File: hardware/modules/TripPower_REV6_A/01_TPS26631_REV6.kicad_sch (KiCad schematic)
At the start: 13 parts, among them Q201 SQM100N10-10_GE3 100V AEC, Q202 BSS138LT1G DRIVER PULLDOWN, U201 TPS26631PWPR

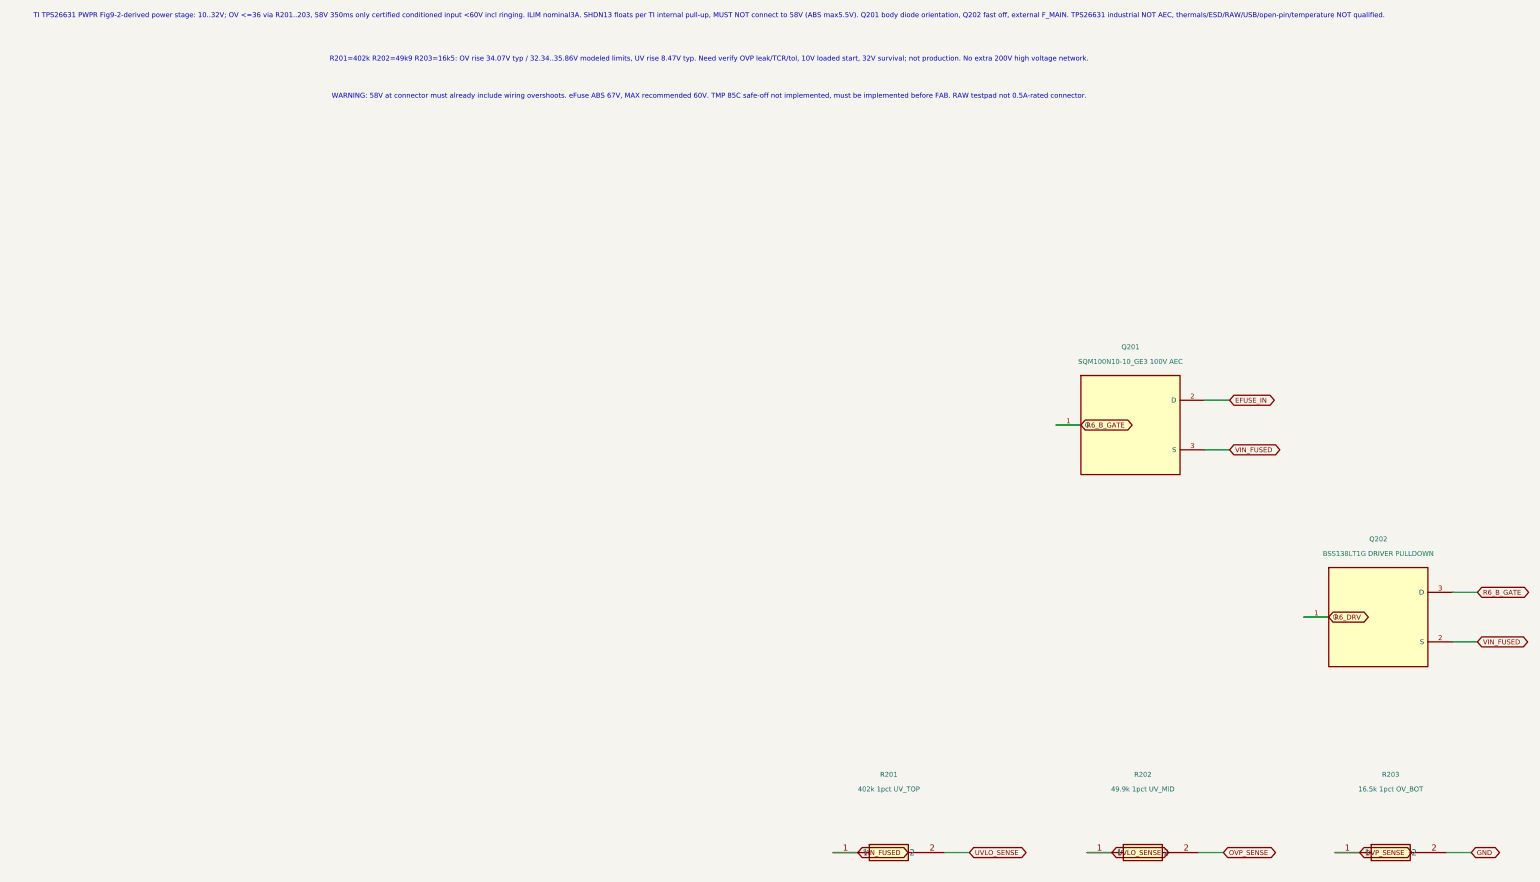
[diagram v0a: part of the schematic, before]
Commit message: Weg A REV6: replace 1% OV divider with available Yageo 0.1% 25ppm 100k/12k4/4k22 to permit verified static 32V OV restart
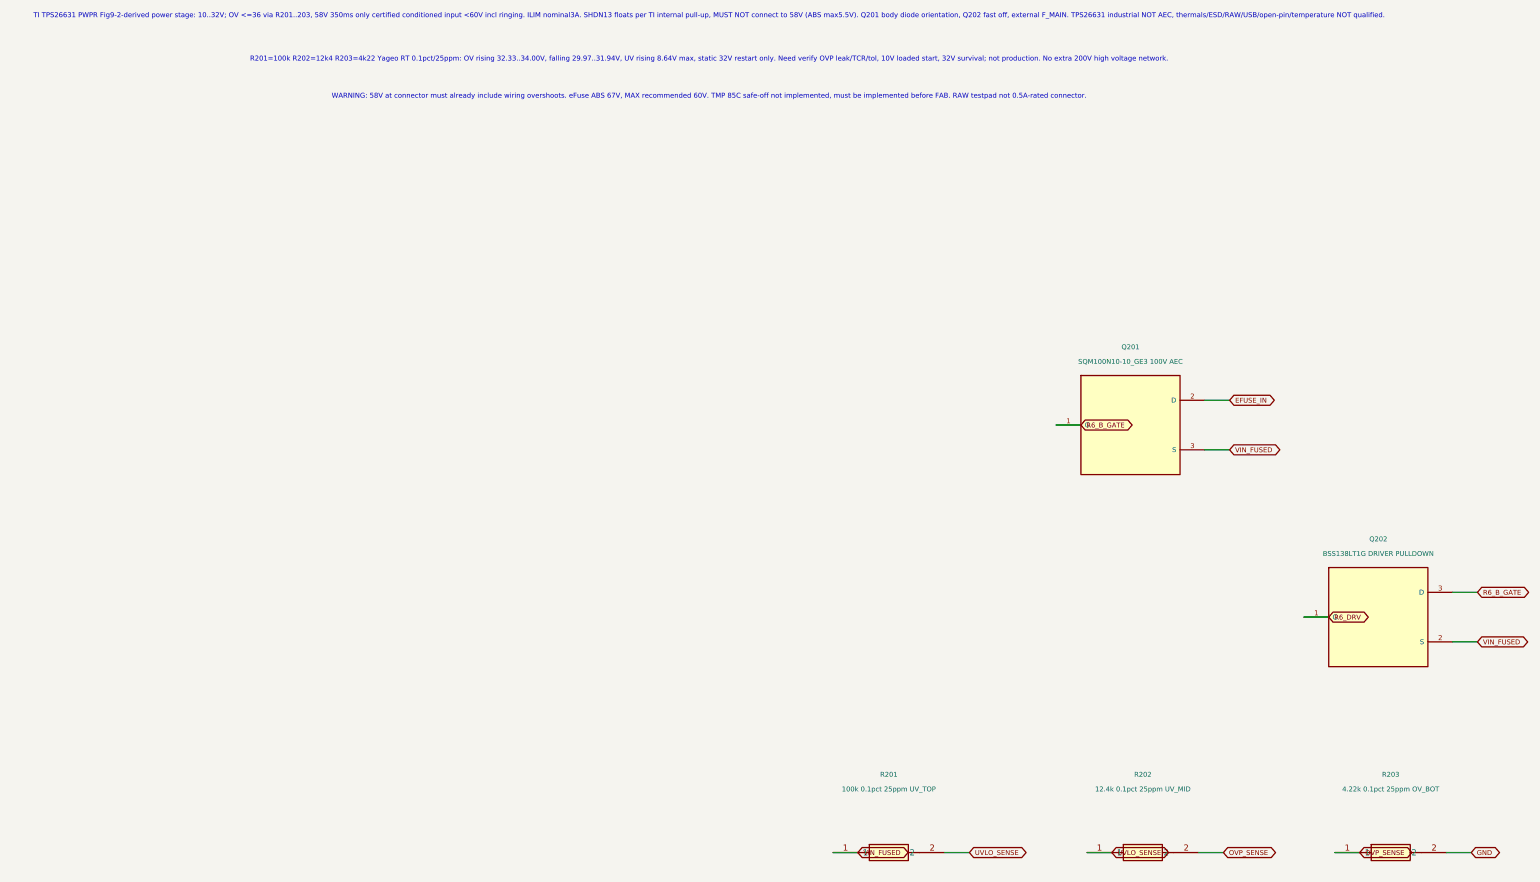
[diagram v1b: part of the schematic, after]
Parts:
- R201: value 402k 1pct UV_TOP -> 100k 0.1pct 25ppm UV_TOP; MPN AC1206FR-07402KL -> RT1206BRD07100KL
- R202: value 49.9k 1pct UV_MID -> 12.4k 0.1pct 25ppm UV_MID; MPN AC1206FR-0749K9L -> RT1206BRD0712K4L
- R203: value 16.5k 1pct OV_BOT -> 4.22k 0.1pct 25ppm OV_BOT; MPN AC1206FR-0716K5L -> RT1206BRD074K22L
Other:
- note added: "R201=100k R202=12k4 R203=4k22 Yageo RT 0.1pct/25ppm: OV rising 32.33..34.00V, falling 29.97..31.94V, UV rising 8.64V max, static 32V restart only. Need verify OVP leak/TCR/tol, 10V loaded start, 32V survival; not production. No extra 200V high voltage network."
- note removed: "R201=402k R202=49k9 R203=16k5: OV rise 34.07V typ / 32.34..35.86V modeled limits, UV rise 8.47V typ. Need verify OVP leak/TCR/tol, 10V loaded start, 32V survival; not production. No extra 200V high voltage network."
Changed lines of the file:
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@@
 (title_block (title "TripPower REV6 A - TPS26631 60V eFuse and 100V reverse FET") (date "2026-10-15") (rev "SCHEMATIC EXPERIMENT / NO FAB"))
 (text "TI TPS26631 PWPR Fig9-2-derived power stage: 10..32V; OV <=36 via R201..203, 58V 350ms only certified conditioned input <60V incl ringing. ILIM nominal3A. SHDN13 floats per TI internal pull-up, MUST NOT connect to 58V (ABS max5.5V). Q201 body diode orientation, Q202 fast off, external F_MAIN. TPS26631 industrial NOT AEC, thermals/ESD/RAW/USB/open-pin/temperature NOT qualified." (at 27.94 34.29 0) (effects (font (size 1.016 1.016))))
-(text "R201=402k R202=49k9 R203=16k5: OV rise 34.07V typ / 32.34..35.86V modeled limits, UV rise 8.47V typ. Need verify OVP leak/TCR/tol, 10V loaded start, 32V survival; not production. No extra 200V high voltage network." (at 27.94 43.18 0) (effects (font (size 1.016 1.016))))
+(text "R201=100k R202=12k4 R203=4k22 Yageo RT 0.1pct/25ppm: OV rising 32.33..34.00V, falling 29.97..31.94V, UV rising 8.64V max, static 32V restart only. Need verify OVP leak/TCR/tol, 10V loaded start, 32V survival; not production. No extra 200V high voltage network." (at 27.94 43.18 0) (effects (font (size 1.016 1.016))))
 (text "WARNING: 58V at connector must already include wiring overshoots. eFuse ABS 67V, MAX recommended 60V. TMP 85C safe-off not implemented, must be implemented before FAB. RAW testpad not 0.5A-rated connector." (at 27.94 50.8 0) (effects (font (size 1.016 1.016))))
 (symbol (lib_id "TripPower_REV6:TPS26631_PWP20") (at 248.92 127 0) (unit 1) (in_bom yes) (on_board yes) (dnp no)
@@
 (symbol (lib_id "Tripmaster_Sym:R") (at 64.77 205.74 0) (unit 1) (in_bom yes) (on_board yes) (dnp no)
 (property "Reference" "R201" (at 64.77 189.74 0) (effects (font (size 1 1))))
-(property "Value" "402k 1pct UV_TOP" (at 64.77 192.74 0) (effects (font (size 1 1))))
+(property "Value" "100k 0.1pct 25ppm UV_TOP" (at 64.77 192.74 0) (effects (font (size 1 1))))
 (property "Footprint" "Resistor_SMD:R_1206_3216Metric" (at 64.77 205.74 0) (effects (font (size 1 1)) (hide yes)))
-(property "MPN" "AC1206FR-07402KL" (at 0 0 0) (effects (font (size 1 1)) (hide yes)))
+(property "MPN" "RT1206BRD07100KL" (at 0 0 0) (effects (font (size 1 1)) (hide yes)))
 (pin "1")
 (pin "2")
@@
 (symbol (lib_id "Tripmaster_Sym:R") (at 116.84 205.74 0) (unit 1) (in_bom yes) (on_board yes) (dnp no)
 (property "Reference" "R202" (at 116.84 189.74 0) (effects (font (size 1 1))))
-(property "Value" "49.9k 1pct UV_MID" (at 116.84 192.74 0) (effects (font (size 1 1))))
+(property "Value" "12.4k 0.1pct 25ppm UV_MID" (at 116.84 192.74 0) (effects (font (size 1 1))))
 (property "Footprint" "Resistor_SMD:R_1206_3216Metric" (at 116.84 205.74 0) (effects (font (size 1 1)) (hide yes)))
-(property "MPN" "AC1206FR-0749K9L" (at 0 0 0) (effects (font (size 1 1)) (hide yes)))
+(property "MPN" "RT1206BRD0712K4L" (at 0 0 0) (effects (font (size 1 1)) (hide yes)))
 (pin "1")
 (pin "2")
@@
 (symbol (lib_id "Tripmaster_Sym:R") (at 167.64 205.74 0) (unit 1) (in_bom yes) (on_board yes) (dnp no)
 (property "Reference" "R203" (at 167.64 189.74 0) (effects (font (size 1 1))))
-(property "Value" "16.5k 1pct OV_BOT" (at 167.64 192.74 0) (effects (font (size 1 1))))
+(property "Value" "4.22k 0.1pct 25ppm OV_BOT" (at 167.64 192.74 0) (effects (font (size 1 1))))
 (property "Footprint" "Resistor_SMD:R_1206_3216Metric" (at 167.64 205.74 0) (effects (font (size 1 1)) (hide yes)))
-(property "MPN" "AC1206FR-0716K5L" (at 0 0 0) (effects (font (size 1 1)) (hide yes)))
+(property "MPN" "RT1206BRD074K22L" (at 0 0 0) (effects (font (size 1 1)) (hide yes)))
 (pin "1")
 (pin "2")

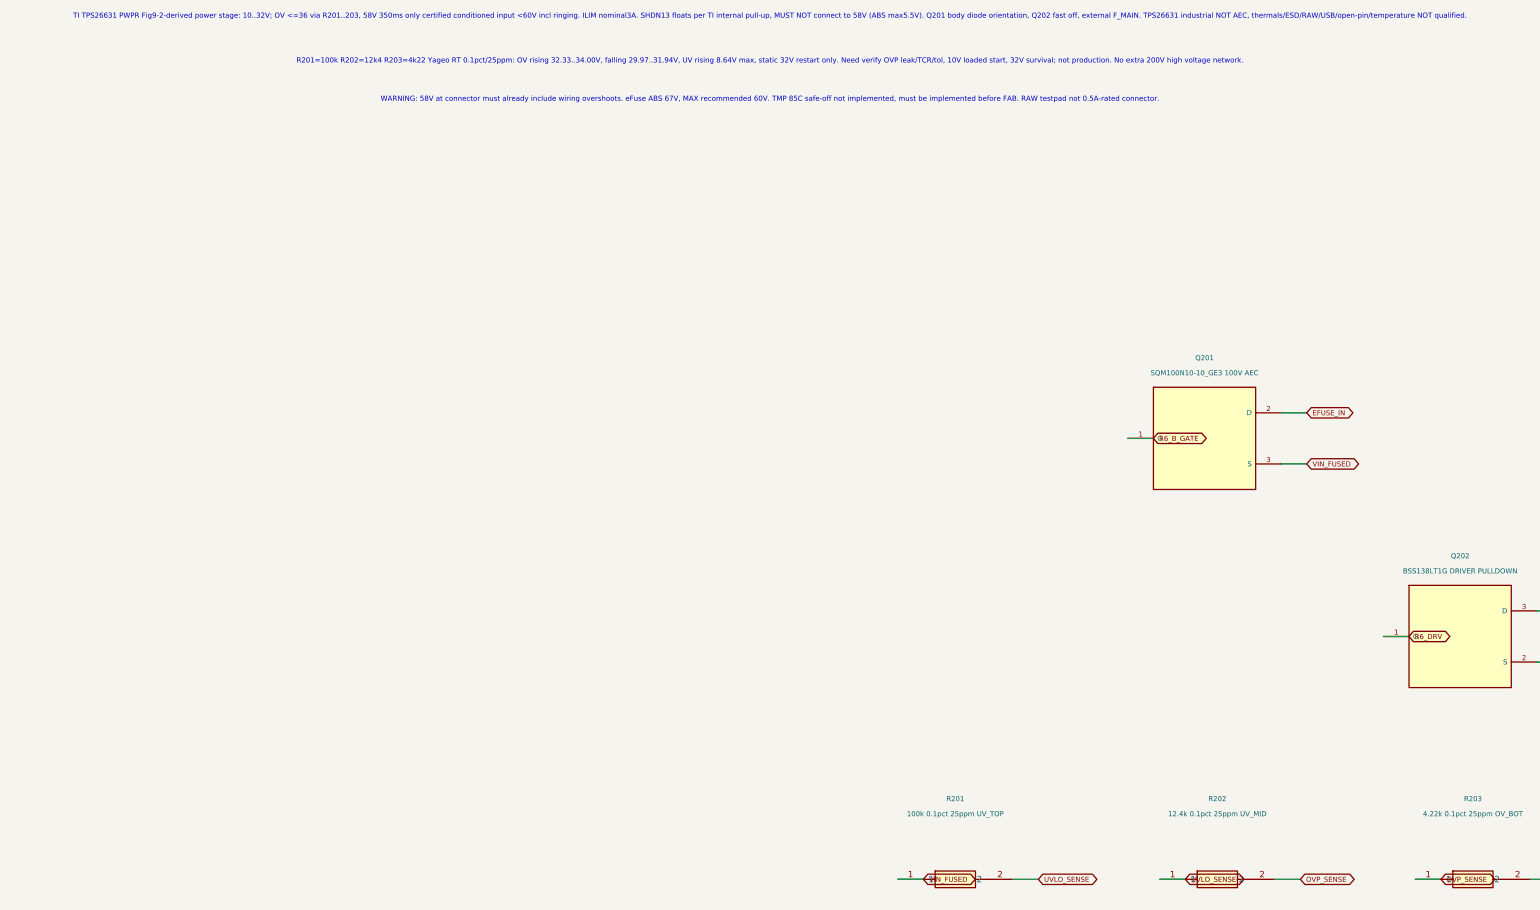
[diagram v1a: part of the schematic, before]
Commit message: TripPower REV6 A: improve 32V OVP return margin using stocked Yageo precision 12k R202 without adding fitted parts
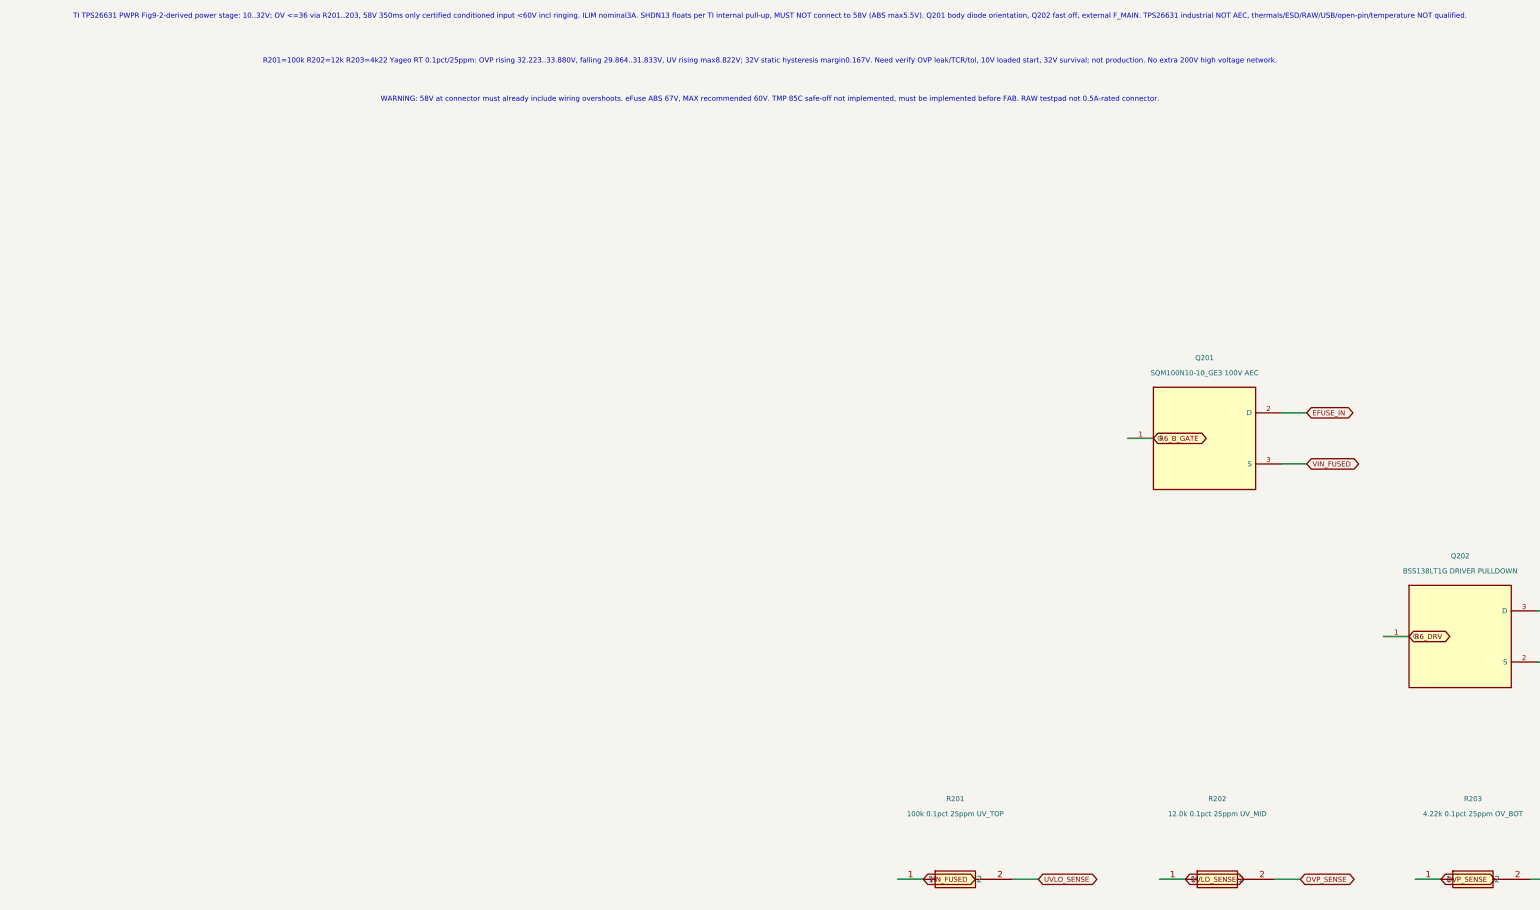
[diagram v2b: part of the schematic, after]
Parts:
- R202: value 12.4k 0.1pct 25ppm UV_MID -> 12.0k 0.1pct 25ppm UV_MID; MPN RT1206BRD0712K4L -> RT1206BRD0712KL
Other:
- note added: "R201=100k R202=12k R203=4k22 Yageo RT 0.1pct/25ppm: OVP rising 32.223..33.880V, falling 29.864..31.833V, UV rising max8.822V; 32V static hysteresis margin0.167V. Need verify OVP leak/TCR/tol, 10V loaded start, 32V survival; not production. No extra 200V high voltage network."
- note removed: "R201=100k R202=12k4 R203=4k22 Yageo RT 0.1pct/25ppm: OV rising 32.33..34.00V, falling 29.97..31.94V, UV rising 8.64V max, static 32V restart only. Need verify OVP leak/TCR/tol, 10V loaded start, 32V survival; not production. No extra 200V high voltage network."
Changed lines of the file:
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@@
 (title_block (title "TripPower REV6 A - TPS26631 60V eFuse and 100V reverse FET") (date "2026-10-15") (rev "SCHEMATIC EXPERIMENT / NO FAB"))
 (text "TI TPS26631 PWPR Fig9-2-derived power stage: 10..32V; OV <=36 via R201..203, 58V 350ms only certified conditioned input <60V incl ringing. ILIM nominal3A. SHDN13 floats per TI internal pull-up, MUST NOT connect to 58V (ABS max5.5V). Q201 body diode orientation, Q202 fast off, external F_MAIN. TPS26631 industrial NOT AEC, thermals/ESD/RAW/USB/open-pin/temperature NOT qualified." (at 27.94 34.29 0) (effects (font (size 1.016 1.016))))
-(text "R201=100k R202=12k4 R203=4k22 Yageo RT 0.1pct/25ppm: OV rising 32.33..34.00V, falling 29.97..31.94V, UV rising 8.64V max, static 32V restart only. Need verify OVP leak/TCR/tol, 10V loaded start, 32V survival; not production. No extra 200V high voltage network." (at 27.94 43.18 0) (effects (font (size 1.016 1.016))))
+(text "R201=100k R202=12k R203=4k22 Yageo RT 0.1pct/25ppm: OVP rising 32.223..33.880V, falling 29.864..31.833V, UV rising max8.822V; 32V static hysteresis margin0.167V. Need verify OVP leak/TCR/tol, 10V loaded start, 32V survival; not production. No extra 200V high voltage network." (at 27.94 43.18 0) (effects (font (size 1.016 1.016))))
 (text "WARNING: 58V at connector must already include wiring overshoots. eFuse ABS 67V, MAX recommended 60V. TMP 85C safe-off not implemented, must be implemented before FAB. RAW testpad not 0.5A-rated connector." (at 27.94 50.8 0) (effects (font (size 1.016 1.016))))
 (symbol (lib_id "TripPower_REV6:TPS26631_PWP20") (at 248.92 127 0) (unit 1) (in_bom yes) (on_board yes) (dnp no)
@@
 (symbol (lib_id "Tripmaster_Sym:R") (at 116.84 205.74 0) (unit 1) (in_bom yes) (on_board yes) (dnp no)
 (property "Reference" "R202" (at 116.84 189.74 0) (effects (font (size 1 1))))
-(property "Value" "12.4k 0.1pct 25ppm UV_MID" (at 116.84 192.74 0) (effects (font (size 1 1))))
+(property "Value" "12.0k 0.1pct 25ppm UV_MID" (at 116.84 192.74 0) (effects (font (size 1 1))))
 (property "Footprint" "Resistor_SMD:R_1206_3216Metric" (at 116.84 205.74 0) (effects (font (size 1 1)) (hide yes)))
-(property "MPN" "RT1206BRD0712K4L" (at 0 0 0) (effects (font (size 1 1)) (hide yes)))
+(property "MPN" "RT1206BRD0712KL" (at 0 0 0) (effects (font (size 1 1)) (hide yes)))
 (pin "1")
 (pin "2")

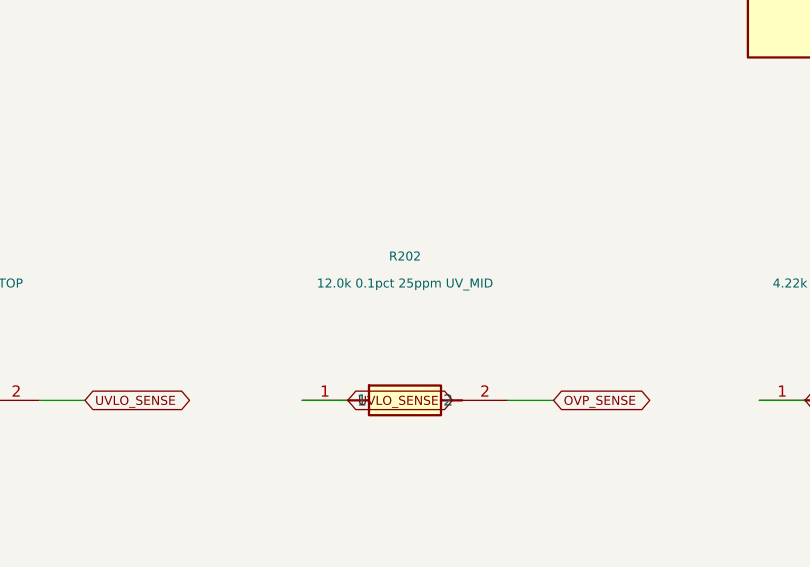
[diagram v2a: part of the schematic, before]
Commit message: REV6 A: adopt stocked Panasonic AEC-Q200 12k/0.1%/25ppm OV precision part 01_TPS26631_REV6.kicad_sch
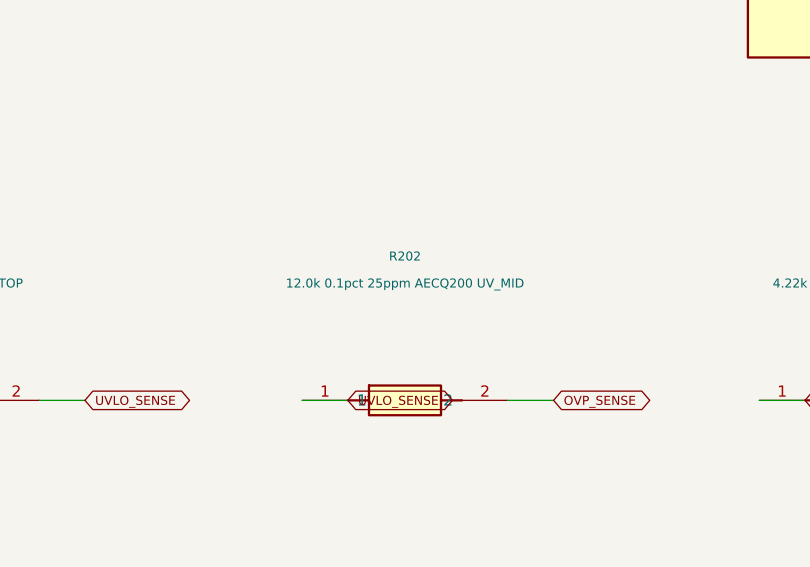
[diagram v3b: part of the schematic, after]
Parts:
- R202: value 12.0k 0.1pct 25ppm UV_MID -> 12.0k 0.1pct 25ppm AECQ200 UV_MID; MPN RT1206BRD0712KL -> ERA-8AEB123V
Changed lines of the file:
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@@
 (symbol (lib_id "Tripmaster_Sym:R") (at 116.84 205.74 0) (unit 1) (in_bom yes) (on_board yes) (dnp no)
 (property "Reference" "R202" (at 116.84 189.74 0) (effects (font (size 1 1))))
-(property "Value" "12.0k 0.1pct 25ppm UV_MID" (at 116.84 192.74 0) (effects (font (size 1 1))))
+(property "Value" "12.0k 0.1pct 25ppm AECQ200 UV_MID" (at 116.84 192.74 0) (effects (font (size 1 1))))
 (property "Footprint" "Resistor_SMD:R_1206_3216Metric" (at 116.84 205.74 0) (effects (font (size 1 1)) (hide yes)))
-(property "MPN" "RT1206BRD0712KL" (at 0 0 0) (effects (font (size 1 1)) (hide yes)))
+(property "MPN" "ERA-8AEB123V" (at 0 0 0) (effects (font (size 1 1)) (hide yes)))
 (pin "1")
 (pin "2")
